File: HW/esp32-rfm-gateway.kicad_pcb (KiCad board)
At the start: 2 copper layers, 48 parts, among them J1 PinsI2C, J2 PinDbg, J20 MicroUSB-B, J3 PinsGP, J30 Ant, Q20 IRLML2244, SW1 BootBtn, U1 ESP-WROOM-32, U2 BD48K30, U20 MCP73831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

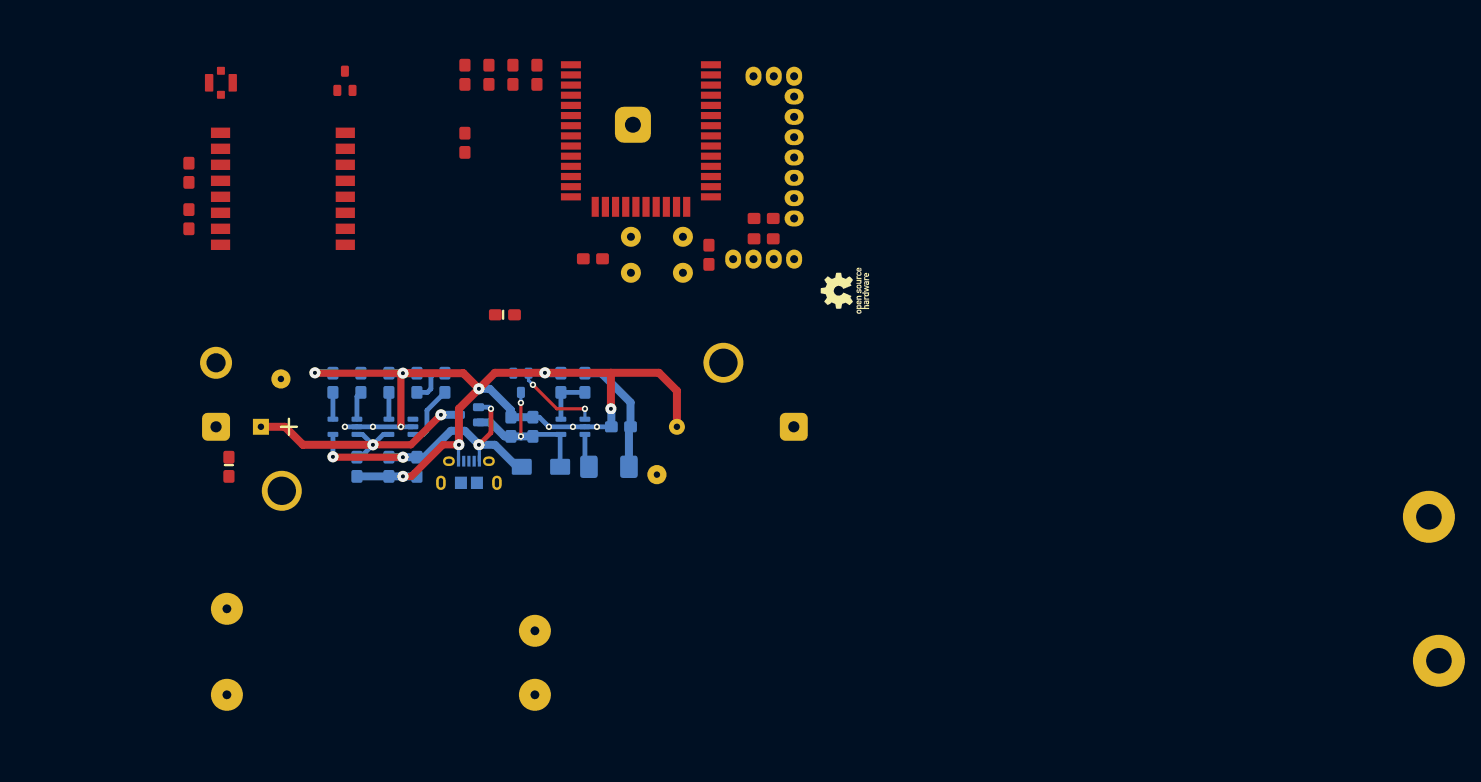
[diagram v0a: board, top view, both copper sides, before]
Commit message: Positions the components, almost ...
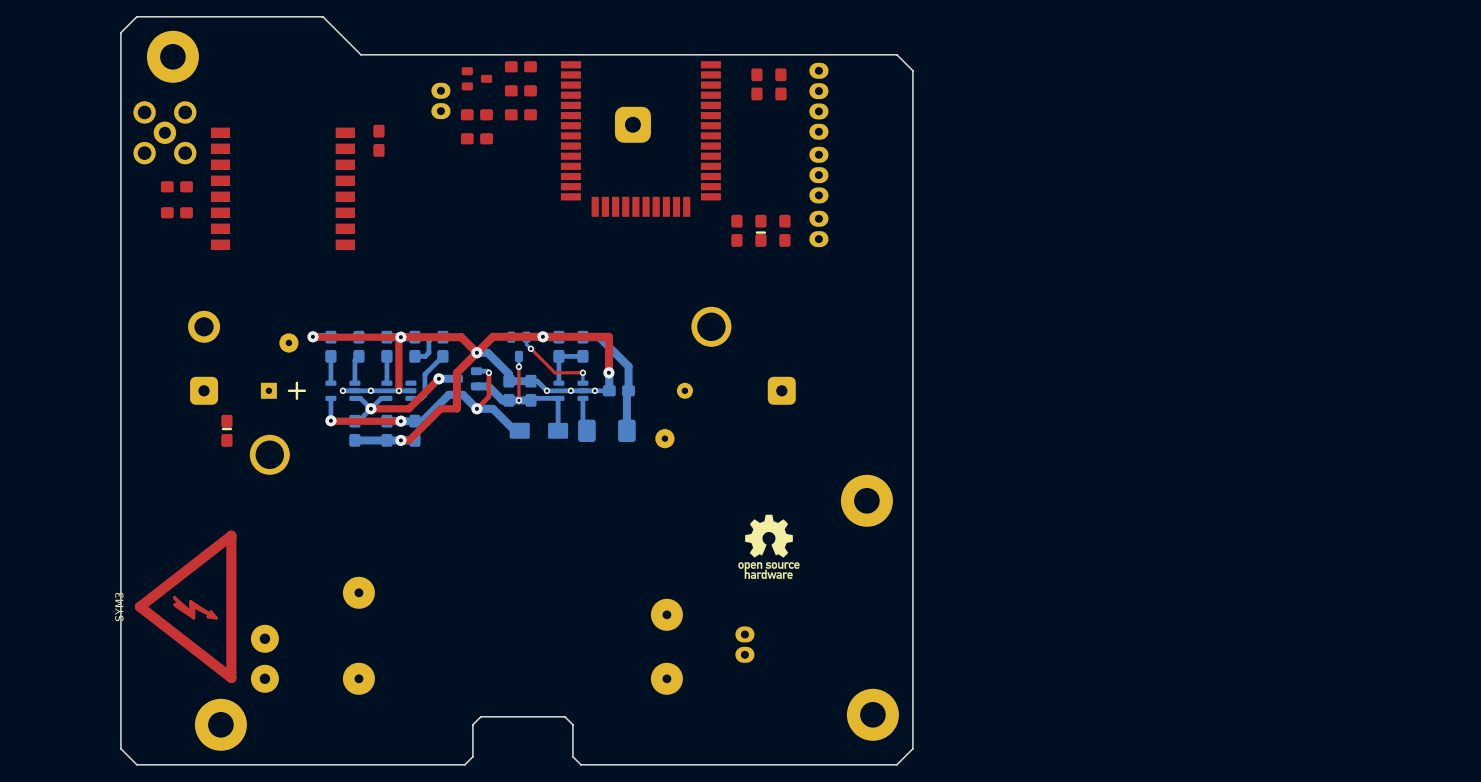
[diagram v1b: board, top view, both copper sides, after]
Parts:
- removed BT1: LiIon, CalinConnectors:BattHolder-AA-PCB
- removed the REF** at (84.0, 95.0)
- removed the REF** at (68.5, 119.2)
- removed SW1: BootBtn, CalinGeneric:SW-Push-4
- added C5: 100nF, CalinGeneric:C0805HS, F.Cu at (80.5, 59.0)
- added H3: Hole, CalinGeneric:HoleNPT-M3, F.Cu at (130.0, 131.0)
- added H4: Hole, CalinGeneric:HoleNPT-M3, F.Cu at (129.2, 104.2)
- added J21: c5V, CalinConnectors:Pin_Header_Straight_1x02, F.Cu at (114.0, 121.0)
- added J22: s14500, CalinConnectors:BattHolder-AA-PCB, F.Cu at (80.5, 90.5)
- added J23: s18650, CalinConnectors:KEYS-1043, F.Cu at (82.5, 90.5)
- added J4: PinsI2C, CalinConnectors:Pin_Header_Straight_1x04, F.Cu at (123.2, 50.5)
- added REF**: G706, CalinBoxes:G706, F.Cu at (86.0, 76.8)
- added SYM3: High Voltage !, Symbol:Symbol_Highvoltage_Type2_CopperTop_Small, F.Cu at (46.0, 117.5)
- added U24: IRM-05, CalinGeneric:IRM222A, F.Cu at (85.0, 117.2)
- J1: value PinsI2C -> Res; footprint CalinConnectors:Pin_Header_Straight_1x04 -> CalinConnectors:Pin_Header_Straight_1x02
- J2: value PinDbg -> Boot; footprint CalinConnectors:Pin_Header_Straight_1x03 -> CalinConnectors:Pin_Header_Straight_1x02
- J20: value MicroUSB-B -> 220 V~; footprint CalinConnectors:USB-MicroB-10118194-0x0 -> CalinConnectors:DG301-5-2; moved to F.Cu
- J3: value PinsGP -> PinDbg; footprint CalinConnectors:Pin_Header_Straight_1x07 -> CalinConnectors:Pin_Header_Straight_1x03_Cyan
- J30: value Ant -> AntSMA; footprint CalinConnectors:U.FL -> CalinConnectors:SMA-90
- R2: value 1K -> 330
- SYM2: footprint Symbol:OSHW-Logo_5.7x6mm_SilkScreen -> Symbol:OSHW-Logo_7.5x8mm_SilkScreen
- moved H1 167.2 mm to (42.5, 48.8)
- moved H2 152.5 mm to (48.5, 132.2)
- moved J1 48.9 mm to (76.0, 53.0), turned to 0 degrees
- moved D1 33.7 mm to (116.0, 70.5), turned to 90 degrees
- moved J20 33.7 mm to (54.0, 124.0), turned to 270 degrees
- moved SYM2 33.4 mm to (117.0, 110.0), turned to 0 degrees
- moved J2 19.6 mm to (123.2, 69.0), turned to 0 degrees
- moved R4 19.4 mm to (118.5, 52.2), turned to 270 degrees
- moved R2 18.3 mm to (113.0, 70.5), turned to 270 degrees
- moved R3 16.8 mm to (115.5, 52.2), turned to 270 degrees
- moved U2 16.5 mm to (80.5, 51.5), turned to 0 degrees
- moved C30 10.8 mm to (68.2, 59.2)
- moved C4 9.96 mm to (119.0, 70.5)
- moved J30 9.38 mm to (41.5, 58.2), turned to 90 degrees
- moved R1 8.60 mm to (86.0, 56.0), turned to 180 degrees
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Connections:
- net Net-(L21-Pad2) renamed /PwrSW
- J1 pad 1: +3V3 -> /Reset
- J2 pad 1: /U0TXD -> /Boot
- J2 pad 2: /U0RXD -> GND
- J20 pad 1: +5VP -> Net-(J20-Pad1)
- J20 pad 2: (no net) -> Net-(J20-Pad2)
- J3 pad 1: /IO23 -> /U0TXD
- J3 pad 2: /IO19 -> /U0RXD
- J3 pad 3: /IO18 -> GND
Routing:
- net GND: track 132.6 -> 116.8 mm, vias 13 -> 12
- net +BATT: track 35.0 -> 20.1 mm
- net +5VP: track 40.2 -> 38.2 mm
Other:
- board outline added: 99 x 93.5 mm

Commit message: Changes NPTH holes and adds 3 pin AC connector
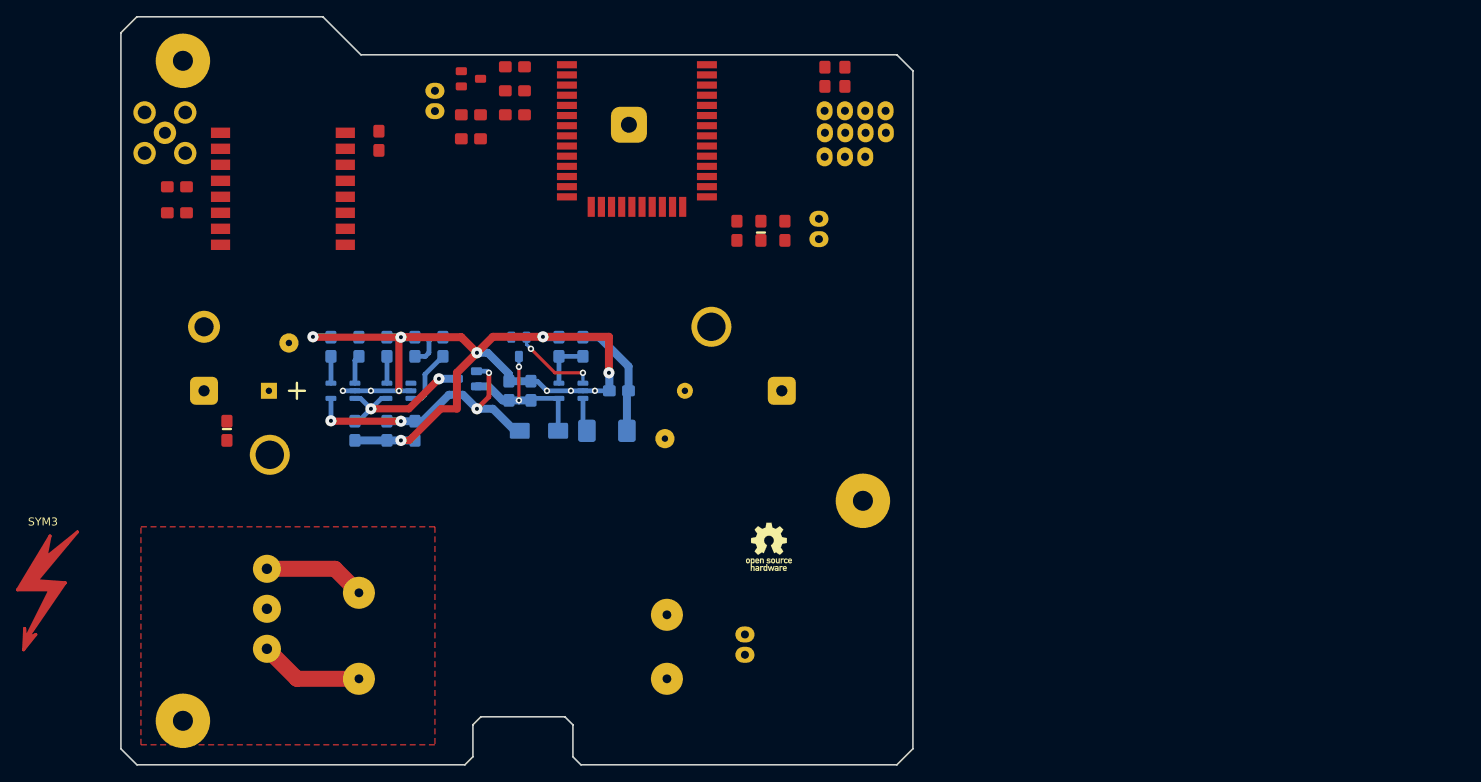
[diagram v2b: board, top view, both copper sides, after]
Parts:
- removed H3: Hole, CalinGeneric:HoleNPT-M3
- removed the REF** at (86.0, 76.8)
- added REF**: Pin_Header_Straight_1x04, CalinConnectors:Pin_Header_Straight_1x04, F.Cu at (124.0, 58.2)
- H1, H2, H4: footprint CalinGeneric:HoleNPT-M3 -> CalinGeneric:HoleNPT-M2.5
- J20: value 220 V~ -> 220V~; footprint CalinConnectors:DG301-5-2 -> CalinConnectors:DG301-5-3
- SYM2: footprint Symbol:OSHW-Logo_7.5x8mm_SilkScreen -> Symbol:OSHW-Logo_5.7x6mm_SilkScreen
- SYM3: footprint Symbol:Symbol_Highvoltage_Type2_CopperTop_Small -> Symbol:Symbol_HighVoltage_Type1_CopperTop_Big
- moved SYM3 19.9 mm to (26.2, 115.0), turned to 0 degrees
- moved J4 9.72 mm to (131.6, 55.5), turned to 270 degrees
- moved R3 8.55 mm to (124.0, 51.2)
- moved R4 8.06 mm to (126.5, 51.2)
- moved J20 6.25 mm to (54.2, 117.8)
- moved H2 4.78 mm to (43.8, 131.8)
- moved H1 1.35 mm to (43.8, 49.2)
- moved J3 0.75 mm to (124.0, 61.2), turned to 90 degrees
- moved C1 0.75 mm to (79.8, 56.0)
- moved C2 0.75 mm to (85.2, 50.0)
- moved C3 0.75 mm to (85.2, 53.0)
- moved C5 0.75 mm to (79.8, 59.0)
- moved J1 0.75 mm to (75.2, 53.0)
- moved R1 0.75 mm to (85.2, 56.0)
- moved U2 0.75 mm to (79.8, 51.5)
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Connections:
- J20 pad 1: Net-(J20-Pad1) -> /ACN
- J20 pad 2: Net-(J20-Pad2) -> (no net)
- U1 pad 27: /U2RXD -> (no net)
- U1 pad 28: /U2TXD -> (no net)
- U1 pad 29: /IO5 -> (no net)
- U1 pad 30: /IO18 -> (no net)
- U1 pad 31: /IO19 -> (no net)
- U1 pad 37: /IO23 -> (no net)
- U24 pad 1: Net-(J20-Pad1) -> /ACL
- U24 pad 2: Net-(J20-Pad2) -> /ACN
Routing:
- net /ACL: track 0.00 -> 13.1 mm
- net /ACN: track 0.00 -> 12.7 mm
- added copper zone on F.Cu, net Earth

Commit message: Creates an Earth plane
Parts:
- removed REF**: Pin_Header_Straight_1x04, CalinConnectors:Pin_Header_Straight_1x04
- added H3: Hole, CalinGeneric:HoleNPT-M2.5, F.Cu at (128.8, 131.8)
- C30, C31, C32: moved to B.Cu
- moved SYM3 16.2 mm to (42.5, 115.0)
- moved C32 12.3 mm to (55.2, 67.8), turned to 0 degrees
- moved C31 12.2 mm to (55.2, 65.0), turned to 0 degrees
- moved C30 10.9 mm to (57.8, 62.2), turned to 180 degrees
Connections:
- J20 pad 2: (no net) -> Earth
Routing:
- net Earth: vias 0 -> 17
- added copper zone on B.Cu, net Earth
- added copper zone on F.Cu, net GND

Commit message: The layout is established
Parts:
- added J5: PinsI2C, CalinConnectors:Pin_Header_Straight_1x04, F.Cu at (130.5, 54.5)
- added SYM4: High Voltage !, Symbol:Symbol_HighVoltage_Type1_CopperTop_Big, B.Cu at (40.2, 117.2)
- C30, C31, C32: moved to F.Cu
- moved C31 12.7 mm to (42.8, 67.2), turned to 180 degrees
- moved C32 12.7 mm to (42.8, 70.0), turned to 180 degrees
- moved C30 11.7 mm to (69.0, 59.0)
- moved J3 8.98 mm to (132.0, 65.2), turned to 0 degrees
- moved J4 3.72 mm to (128.0, 54.5), turned to 0 degrees
- moved R3 2.50 mm to (121.5, 51.2)
- moved R4 2.50 mm to (124.0, 51.2)
- moved J30 1.03 mm to (41.2, 59.2)
- moved U30 1.00 mm to (56.2, 66.2)
- moved SYM3 0.56 mm to (42.2, 115.5)
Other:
- outline, holes or cut-outs redrawn

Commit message: The margins are established
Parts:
- moved D20 8.78 mm to (40.5, 96.2)
- moved Q20 1.50 mm to (79.2, 90.5)
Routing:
- net GND: track 116.8 -> 90.9 mm
- net +5VP: track 38.2 -> 37.0 mm
- net /VinReg: track 20.7 -> 20.1 mm
- net +BATT: track 20.1 -> 19.5 mm

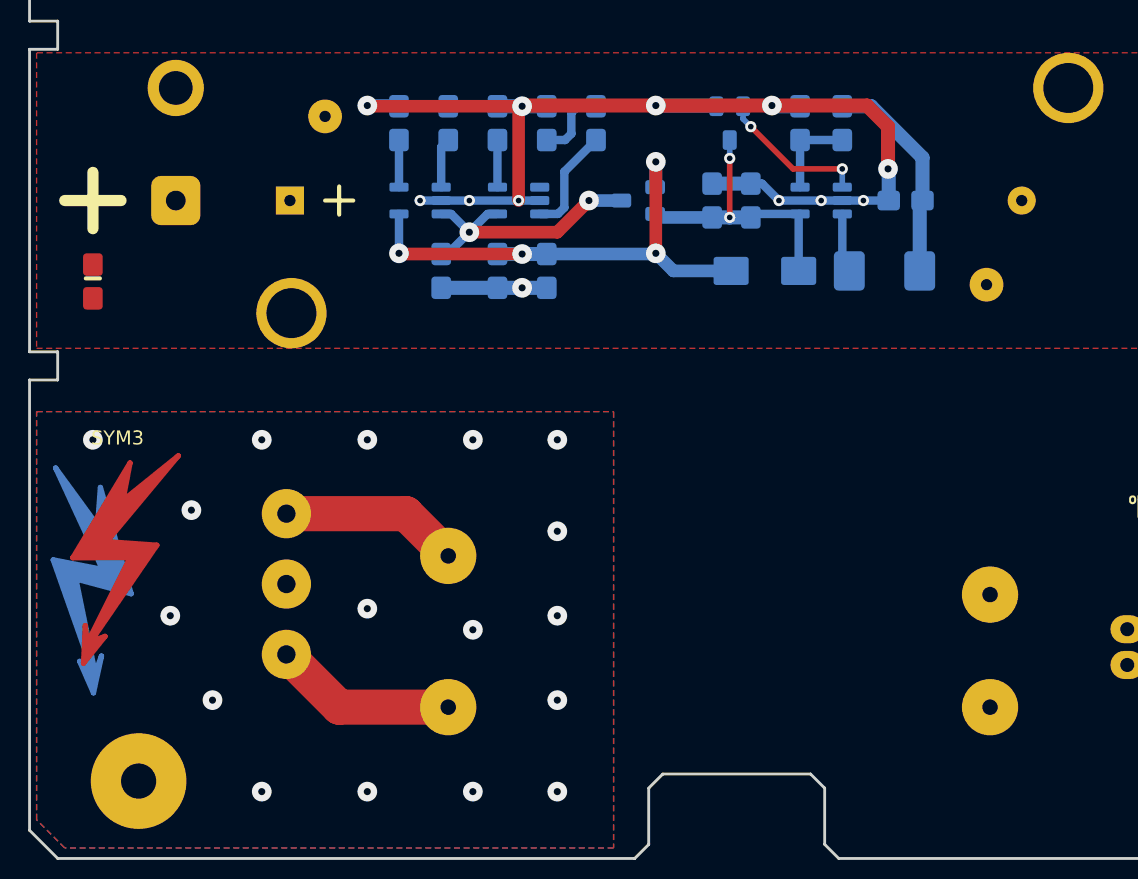
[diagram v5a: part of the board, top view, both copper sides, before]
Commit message: Repositions many components of the power section
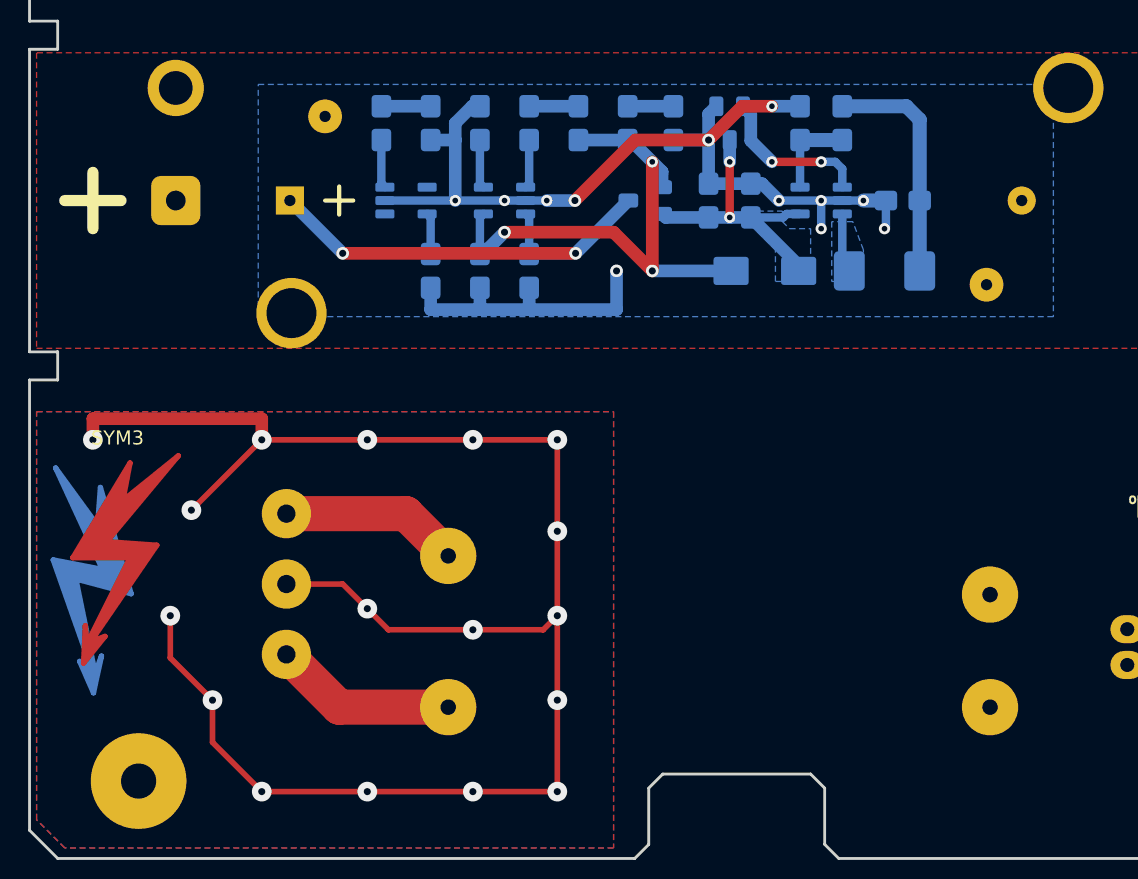
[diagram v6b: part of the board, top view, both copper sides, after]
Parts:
- added R28: 100k 1%, CalinGeneric:R0805HS, B.Cu at (90.8, 85.0)
- D20: moved to B.Cu
- R21: value 1K -> 330
- R26: value 442k 1% -> 10k
- R27: value 100k 1% -> 442k 1%
- U20: value MCP73831 -> IRM-05; footprint CalinGeneric:SOT-23-5-HS -> CalinGeneric:IRM222A; moved to F.Cu
- U21: value AP2280-1WG-7 -> MCP73832T-2ACI
- U24: value IRM-05 -> AP2280-1WG-7; footprint CalinGeneric:IRM222A -> CalinGeneric:SOT-23-5-HS; moved to B.Cu
- moved D20 36.3 mm to (75.0, 85.0)
- moved U24 34.8 mm to (62.8, 90.5), turned to 0 degrees
- moved U20 34.2 mm to (85.0, 117.2)
- moved R23 15.2 mm to (61.0, 85.0)
- moved R26 12.0 mm to (81.8, 85.0)
- moved R25 12.0 mm to (78.5, 85.0), turned to 90 degrees
- moved R22 11.5 mm to (64.5, 95.5), turned to 270 degrees
- moved R24 8.25 mm to (64.5, 85.0), turned to 270 degrees
- moved C21 6.25 mm to (71.5, 95.5)
- moved R20 5.75 mm to (68.0, 85.0)
- moved R21 5.75 mm to (71.5, 85.0)
- moved R27 3.00 mm to (93.8, 85.0), turned to 270 degrees
- moved C20 1.25 mm to (68.0, 95.5)
- moved U21 1.00 mm to (69.8, 90.5)
- moved Q20 0.50 mm to (79.8, 90.5)
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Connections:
- net /VinBOR renamed Net-(U22-Pad2)
- R21 pad 1: Net-(R21-Pad1) -> /ChargeStat
- R25 pad 2: GND -> /ADC_Vin
- R26 pad 1: +3V3 -> /ADC_Vin
- R26 pad 2: Net-(R26-Pad2) -> GND
- R27 pad 1: Net-(R26-Pad2) -> +3V3
- R27 pad 2: GND -> Net-(R27-Pad2)
- U1 pad 4: (no net) -> /ADC_Vin
- U20 pad 1: Net-(R21-Pad1) -> /ACL
- U20 pad 2: GND -> /ACN
- U20 pad 3: +BATT -> +5VP
- U20 pad 4: +5VP -> GND
- U21 pad 1: (no net) -> /ChargeStat
- U21 pad 3: Net-(R23-Pad1) -> +BATT
- U21 pad 4: +BATT -> +5VP
- U21 pad 5: /VBatMC -> Net-(R20-Pad1)
- U23 pad 5: Net-(R26-Pad2) -> Net-(R27-Pad2)
- U24 pad 1: /ACL -> (no net)
- U24 pad 2: /ACN -> GND
- U24 pad 3: +5VP -> Net-(R23-Pad1)
- U24 pad 4: GND -> +BATT
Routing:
- net Earth: track 0.00 -> 125.3 mm
- net +BATT: track 19.5 -> 33.4 mm
- net Net-(R27-Pad2): track 0.00 -> 6.35 mm
- net Net-(R26-Pad2): track 6.35 -> 0.00 mm
- net Net-(R23-Pad1): track 7.67 -> 3.45 mm
- net Net-(R21-Pad1): track 3.56 -> 0.00 mm
- net Net-(D20-PadK): track 0.00 -> 3.50 mm
- net /ChargeStat: track 0.00 -> 3.45 mm
- net /ADC_Vin: track 0.00 -> 3.25 mm
- net GND: track 90.9 -> 87.7 mm
- net /ADC_Batt: track 5.37 -> 3.50 mm
- net +3V3: track 15.3 -> 16.6 mm
- net +5VP: track 37.0 -> 38.3 mm, vias 4 -> 3
- net /VinReg: track 20.1 -> 20.7 mm
- net Net-(U22-Pad2): track 10.7 -> 11.3 mm
- added copper zone on B.Cu, net /PwrSW
- added copper zone on B.Cu, net /VinReg
- added copper zone on B.Cu, net GND
